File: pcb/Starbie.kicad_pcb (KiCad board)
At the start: 2 copper layers, 105 x 87 mm, 17 parts, among them J1 Conn_01x04_Pin, J2 Conn_01x08_Pin, SW1 SW_Push, SW2 SW_Push, U1 DHT11, U2 XIAO-ESP32-C3-SMD

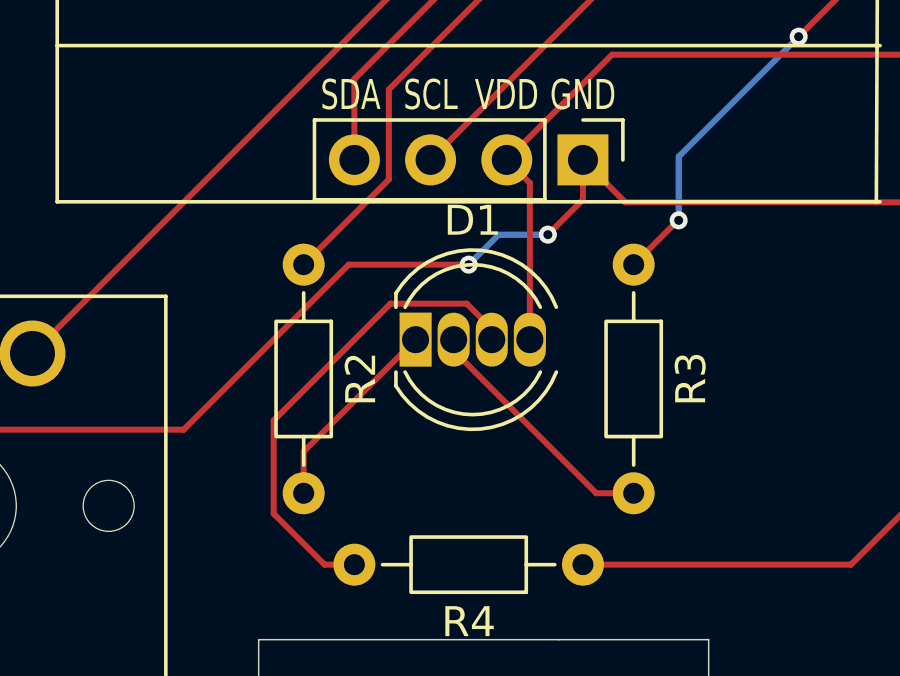
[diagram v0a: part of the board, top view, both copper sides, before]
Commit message: Refactor LED properties and update designators in PCB and schematic files
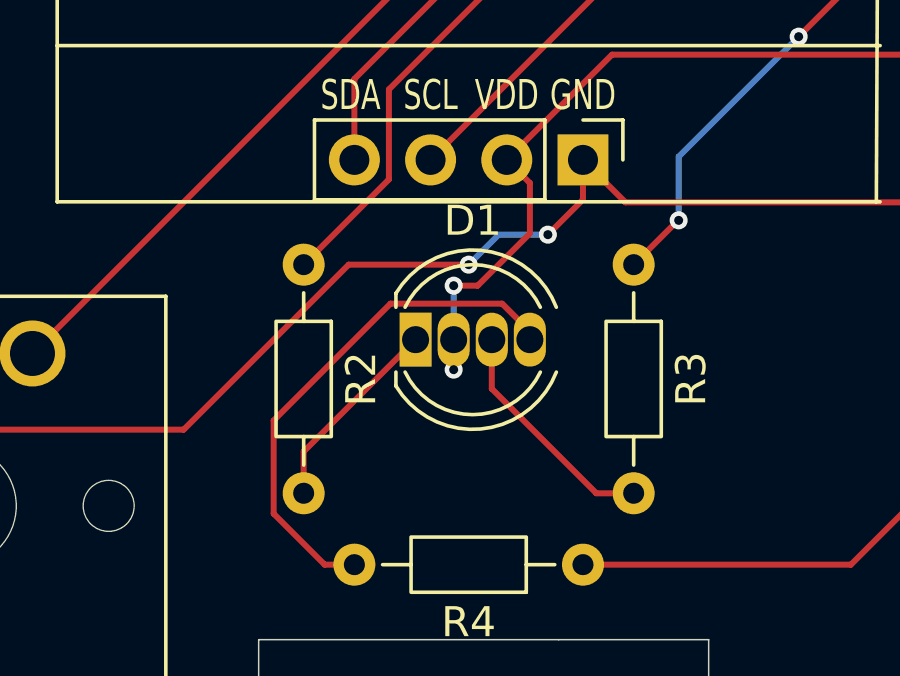
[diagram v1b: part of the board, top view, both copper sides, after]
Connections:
- D1 pad 2: Net-(D1-GK) -> +3.3V
- D1 pad 3: Net-(D1-BK) -> Net-(D1-GK)
- D1 pad 4: +3.3V -> Net-(D1-BK)
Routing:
- net +3.3V: track 101.7 -> 105.3 mm, vias 6 -> 8
- net Net-(D1-BK): track 16.1 -> 17.3 mm
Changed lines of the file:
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@@
 			)
 		)
-		(property "Description" "RGB LED, red/green/blue/anode"
+		(property "Description" "RGB LED, red/anode/green/blue"
 			(at 0 0 0)
 			(layer "F.Fab")
@@
 			(unit
 				(name "A")
-				(pins "1" "2" "3" "4")
+				(pins "1" "3" "4" "2")
 			)
 		)
@@
 			(layers "*.Cu" "*.Mask")
 			(remove_unused_layers no)
-			(net "Net-(D1-GK)")
-			(pinfunction "GK_2")
+			(net "+3.3V")
+			(pinfunction "A_2")
 			(pintype "passive")
 		)
@@
 			(layers "*.Cu" "*.Mask")
 			(remove_unused_layers no)
-			(net "Net-(D1-BK)")
-			(pinfunction "BK_3")
+			(net "Net-(D1-GK)")
+			(pinfunction "GK_3")
 			(pintype "passive")
 		)
@@
 			(layers "*.Cu" "*.Mask")
 			(remove_unused_layers no)
-			(net "+3.3V")
-			(pinfunction "A_4")
+			(net "Net-(D1-BK)")
+			(pinfunction "BK_4")
 			(pintype "passive")
 		)
@@
 	)
 	(segment
-		(start 136.5 121.73)
-		(end 140.23 118)
+		(start 140.23 118)
+		(end 136.5 121.73)
 		(width 0.2)
 		(layer "F.Cu")
@@
 	)
 	(segment
-		(start 141.5 118.365)
-		(end 146.255 123.12)
+		(start 142.77 118)
+		(end 142.77 119.635)
 		(width 0.2)
 		(layer "F.Cu")
@@
 	)
 	(segment
-		(start 146.255 123.12)
-		(end 147.5 123.12)
+		(start 142.77 119.635)
+		(end 146.255 123.12)
 		(width 0.2)
 		(layer "F.Cu")
@@
 	)
 	(segment
-		(start 141.5 118)
-		(end 141.5 118.365)
+		(start 142.77 117.635)
+		(end 142.77 118)
 		(width 0.2)
 		(layer "F.Cu")
@@
 	)
 	(segment
-		(start 141.935 116.8)
-		(end 142.77 117.635)
+		(start 146.255 123.12)
+		(end 147.5 123.12)
 		(width 0.2)
 		(layer "F.Cu")
-		(net "Net-(D1-BK)")
+		(net "Net-(D1-GK)")
 	)
 	(segment
-		(start 139.395 116.8)
-		(end 141.935 116.8)
+		(start 144.04 118)
+		(end 144.04 117.724132)
 		(width 0.2)
 		(layer "F.Cu")
@@
 	)
 	(segment
-		(start 142.77 117.635)
-		(end 142.77 118)
+		(start 144.04 117.724132)
+		(end 143.115868 116.8)
 		(width 0.2)
 		(layer "F.Cu")
@@
 	)
 	(segment
+		(start 143.115868 116.8)
+		(end 139.395 116.8)
+		(width 0.2)
+		(layer "F.Cu")
+		(net "Net-(D1-BK)")
+	)
+	(segment
 		(start 137.200051 125.5)
 		(end 135.5 123.799949)
@@
 	)
 	(segment
+		(start 141.5 116.2)
+		(end 142.3 116.2)
+		(width 0.2)
+		(layer "F.Cu")
+		(net "+3.3V")
+	)
+	(segment
 		(start 146.174265 72.134265)
 		(end 146.54 72.5)
@@
 	)
 	(segment
+		(start 142.3 116.2)
+		(end 144.04 114.46)
+		(width 0.2)
+		(layer "F.Cu")
+		(net "+3.3V")
+	)
+	(segment
 		(start 146.54 72.5)
 		(end 168.88 94.84)
@@
 	)
 	(segment
+		(start 141.5 118)
+		(end 141.5 119)
+		(width 0.2)
+		(layer "F.Cu")
+		(net "+3.3V")
+	)
+	(segment
 		(start 172 109.08853)
 		(end 172.044265 109.044265)
@@
 	)
 	(segment
-		(start 144.04 118)
+		(start 144.04 114.46)
 		(end 144.04 112.778)
 		(width 0.2)
@@
 	)
 	(via
+		(at 141.5 116.2)
+		(size 0.6)
+		(drill 0.3)
+		(layers "F.Cu" "B.Cu")
+		(net "+3.3V")
+	)
+	(via
 		(at 168.545735 108.5)
 		(size 0.6)
@@
 	)
 	(via
+		(at 141.5 119)
+		(size 0.6)
+		(drill 0.3)
+		(layers "F.Cu" "B.Cu")
+		(net "+3.3V")
+	)
+	(via
 		(at 146.174265 71.174265)
 		(size 0.6)
@@
 		(width 0.2)
 		(layer "B.Cu")
+		(net "+3.3V")
+	)
+	(segment
+		(start 141.5 119)
+		(end 141.5 116.2)
+		(width 0.2)
+		(layer "B.Cu")
